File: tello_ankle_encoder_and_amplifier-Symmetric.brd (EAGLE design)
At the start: 30.1 x 61 mm, 43 parts, among them IC1 STM32G431KBU6, IC2 AS5147U-HTSM, IC3 PACDN042Y3R, IC4 PACDN042Y3R, J1 SM04B-GHS-TB(LF)(SN)-, J2 SM02BGHSTBLFSN, J3 SM04B-GHS-TB(LF)(SN)-, J4 SM04B-GHS-TB(LF)(SN)-, J5 5055670271, J6 SM04B-GHS-TB(LF)(SN)-, U1 MCP2562FD-H/MFDFN8_3X3MC_MCH-M, U2 AP7361C-33Y5-13SOT89-5_DIO-M, Y1 ECS-80-18-33-JGN-TR

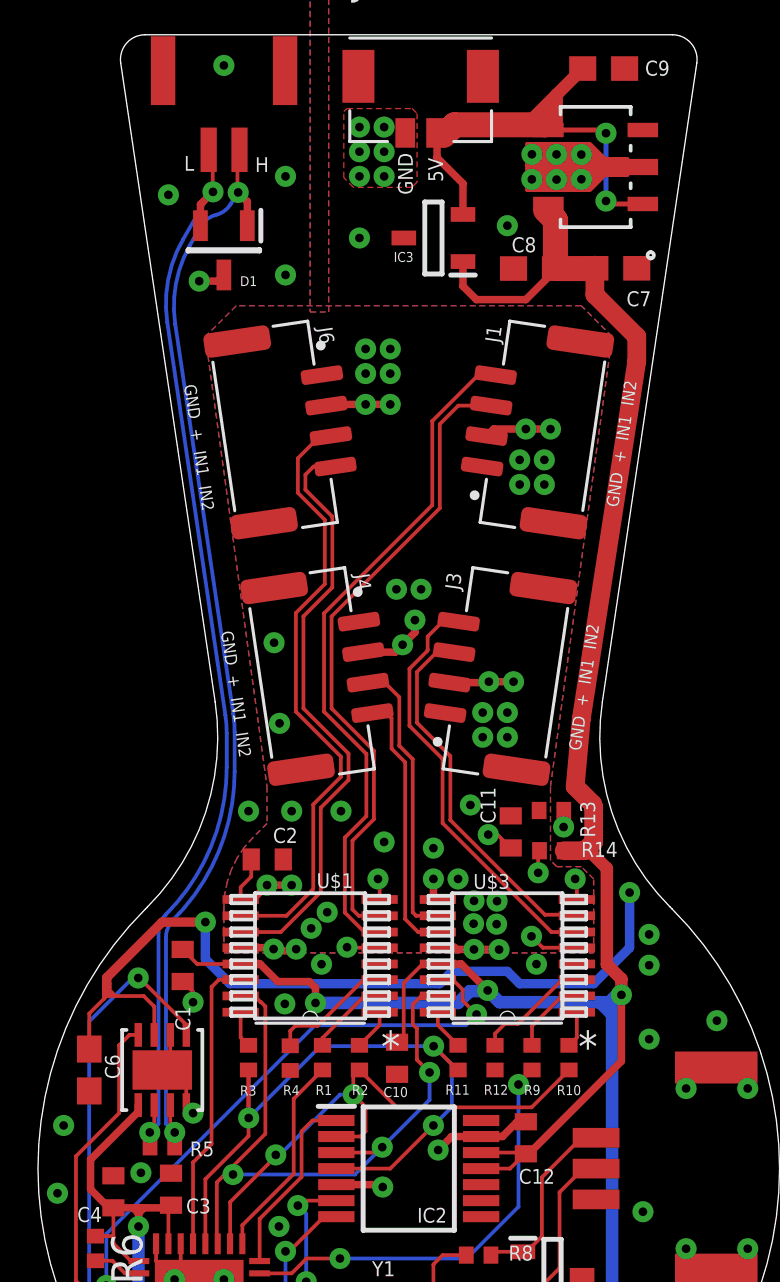
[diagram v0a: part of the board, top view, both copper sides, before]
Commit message: added manufacturing files
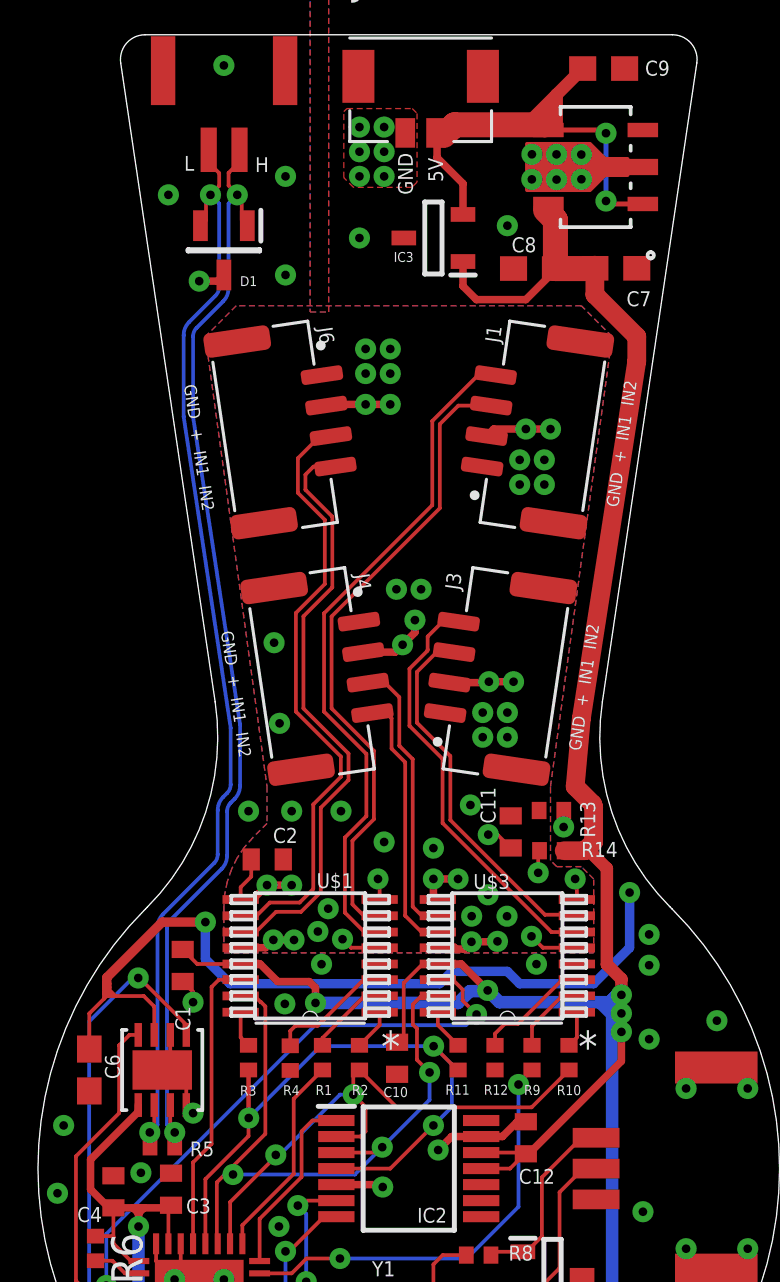
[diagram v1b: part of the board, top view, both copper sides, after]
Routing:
- net AVDD: track 22.8 -> 23.8 mm
- net CAN_N: track 44.6 -> 45.4 mm
- net CAN_P: track 44.9 -> 45.7 mm
- net AGND: track 5.09 -> 5.41 mm, vias 31 -> 30
- net 3V3: vias 5 -> 7
